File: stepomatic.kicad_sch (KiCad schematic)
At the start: 31 parts, among them J1 I2C, J4 USB_B_Micro, Q1 MMBT3904, Q2 MMBT3904, SW1 Mode, SW2 RST, U1 HDC1080DMBR, U2 AMS1117-3.3, U3 ULN2003A, U4 CH340C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

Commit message: Add JLC part for neopixel
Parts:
- D1: LCSC DNP -> C2843785
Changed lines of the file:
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@@
       (effects (font (size 1.27 1.27)) (justify left top) hide)
     )
-    (property "LCSC" "DNP" (id 5) (at 189.23 38.1 0)
+    (property "LCSC" "C2843785" (id 5) (at 189.23 38.1 0)
       (effects (font (size 1.27 1.27)) hide)
     )

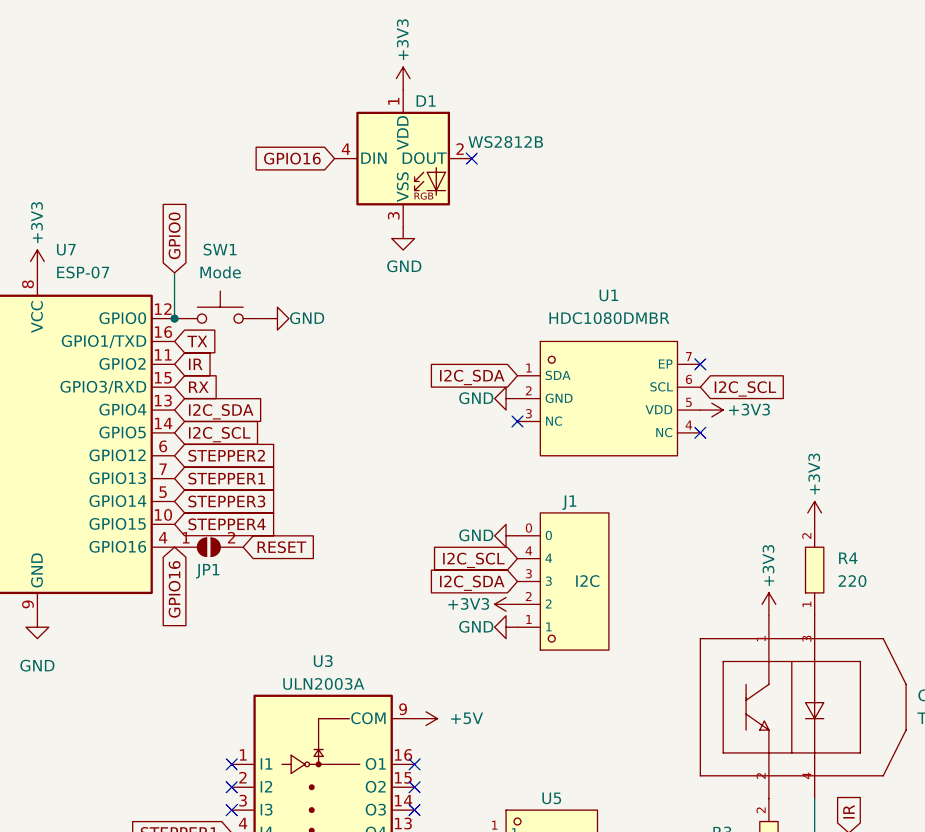
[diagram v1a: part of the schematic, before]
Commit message: Add EP pad of HDC1080DMBR
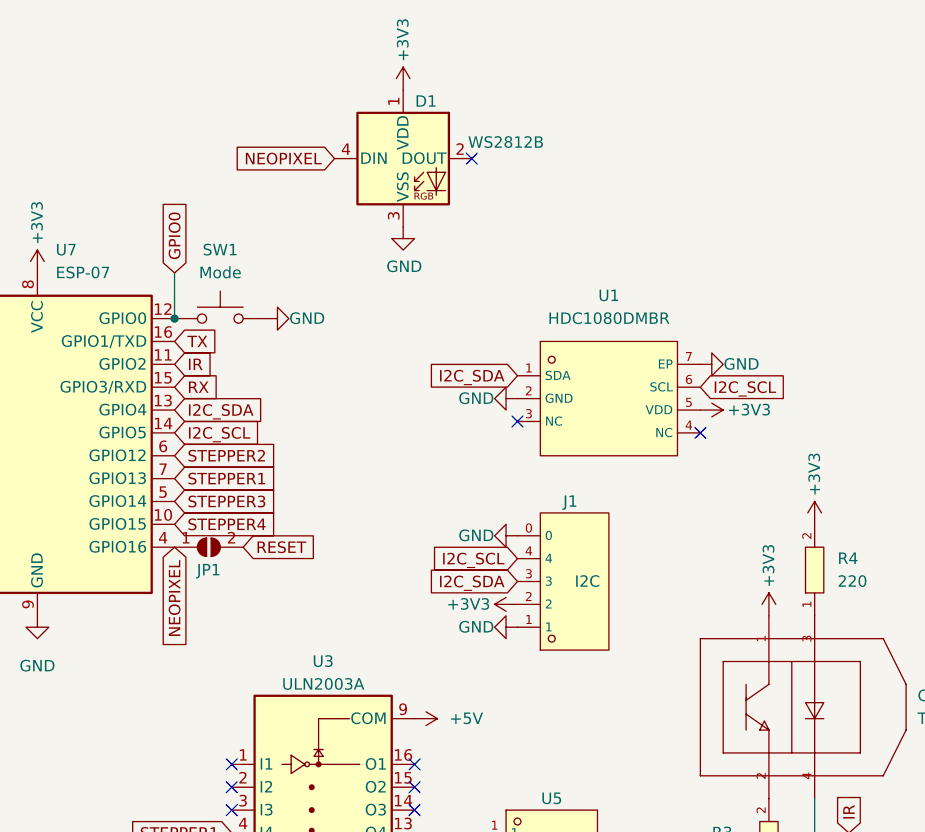
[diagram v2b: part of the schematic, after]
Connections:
- net GND: now also U1.7 (EP)
- net GPIO16 renamed NEOPIXEL
- no-connect marks 17 -> 16
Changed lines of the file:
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@@
   (no_connect (at 190.5 107.95))
   (no_connect (at 222.25 68.58))
-  (no_connect (at 222.25 60.96))
   (no_connect (at 81.28 73.66))
   (no_connect (at 190.5 105.41))
@@
     )
   )
-  (global_label "GPIO16" (shape input) (at 163.83 81.28 270) (fields_autoplaced)
+  (global_label "NEOPIXEL" (shape input) (at 163.83 81.28 270) (fields_autoplaced)
     (effects (font (size 1.27 1.27)) (justify right))
-    (property "Intersheet References" "${INTERSHEET_REFS}" (id 0) (at 163.7506 90.5874 90)
+    (property "Intersheet References" "${INTERSHEET_REFS}" (id 0) (at 163.7506 92.7645 90)
       (effects (font (size 1.27 1.27)) (justify right) hide)
     )
@@
     )
   )
-  (global_label "GPIO16" (shape input) (at 181.61 38.1 180) (fields_autoplaced)
+  (global_label "NEOPIXEL" (shape input) (at 181.61 38.1 180) (fields_autoplaced)
     (effects (font (size 1.27 1.27)) (justify right))
-    (property "Intersheet References" "${INTERSHEET_REFS}" (id 0) (at 172.3026 38.0206 0)
+    (property "Intersheet References" "${INTERSHEET_REFS}" (id 0) (at 170.1255 38.0206 0)
       (effects (font (size 1.27 1.27)) (justify right) hide)
     )
@@
     (pin "4")
   )
+  (symbol (lib_id "power:GND") (at 222.25 60.96 90) (unit 1)
+    (in_bom yes) (on_board yes)
+    (property "Reference" "#PWR0111" (id 0) (at 228.6 60.96 0)
+      (effects (font (size 1.27 1.27)) hide)
+    )
+    (property "Value" "GND" (id 1) (at 226.822 60.96 90))
+    (property "Footprint" "" (id 2) (at 222.25 60.96 0)
+      (effects (font (size 1.27 1.27)) hide)
+    )
+    (property "Datasheet" "" (id 3) (at 222.25 60.96 0)
+      (effects (font (size 1.27 1.27)) hide)
+    )
+    (pin "1")
+  )
   (symbol (lib_id "power:GND") (at 201.93 64.77 270) (unit 1)
     (in_bom yes) (on_board yes)
@@
       (reference "#PWR0110") (unit 1) (value "GND") (footprint "")
     )
+    (path "/f3e5bab0-c824-4fb9-ab63-26b208733bd7"
+      (reference "#PWR0111") (unit 1) (value "GND") (footprint "")
+    )
     (path "/f79577be-2482-43ec-a3db-27da2785cb91"

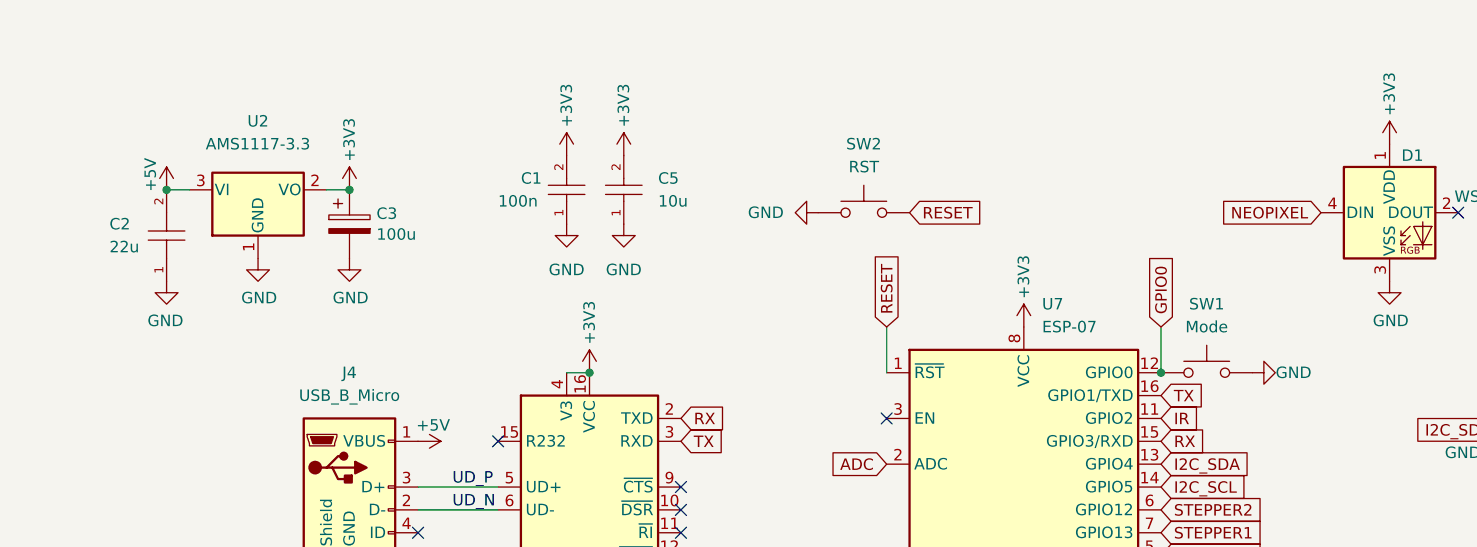
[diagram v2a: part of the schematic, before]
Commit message: Only use JLC footprints
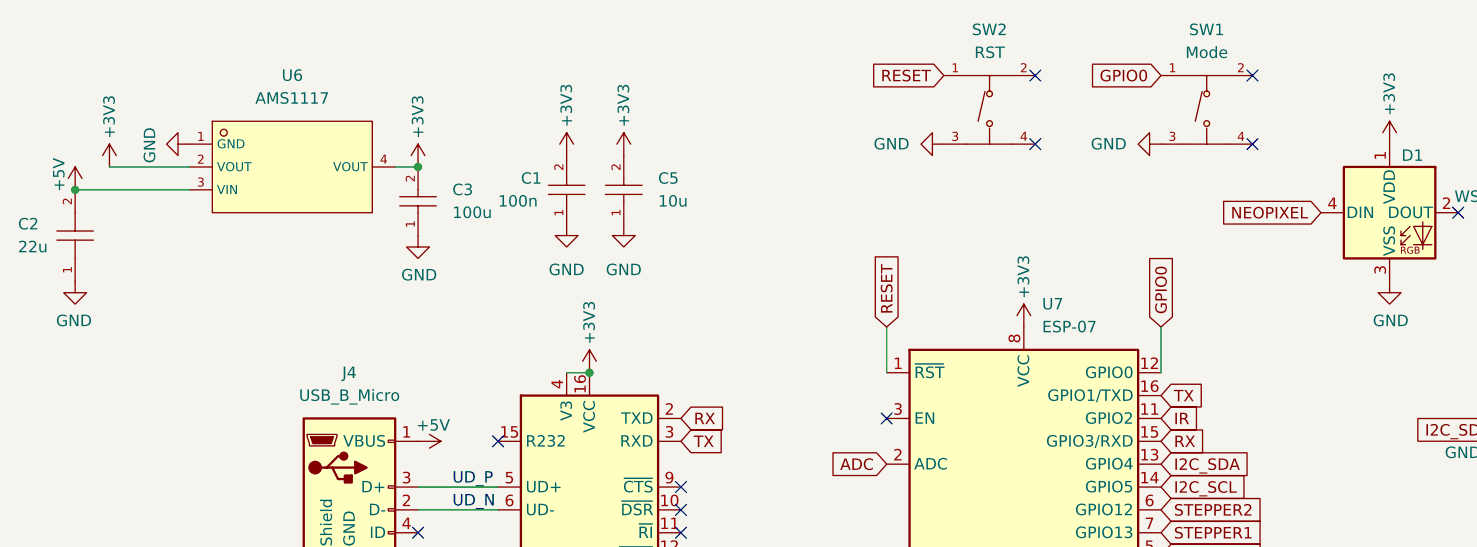
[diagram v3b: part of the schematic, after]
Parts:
- removed C3: 100u, footprint:C1206, symbol ESP-12E-breakout-rescue:CP-Device
- removed SW1: Mode, Button_Switch_SMD:SW_SPST_SKQG_WithoutStem, symbol Switch:SW_Push
- removed SW2: RST, Button_Switch_SMD:SW_SPST_SKQG_WithoutStem, symbol Switch:SW_Push
- removed U2: AMS1117-3.3, Package_TO_SOT_SMD:SOT-223-3_TabPin2, symbol Regulator_Linear:AMS1117-3.3
- added C3: 100u, footprint:C1206, symbol CL31A107MQHNNNE:CL31A107MQHNNNE
- added SW1: Mode, footprint:SW-SMD_4P-L5.1-W5.1-P3.70-LS6.5-TL-2, symbol TS-1187A-B-A-B:TS-1187A-B-A-B
- added SW2: RST, footprint:SW-SMD_4P-L5.1-W5.1-P3.70-LS6.5-TL-2, symbol TS-1187A-B-A-B:TS-1187A-B-A-B
- added U6: AMS1117, footprint:SOT-223-3_L6.5-W3.4-P2.30-LS7.0-BR, symbol AMS1117-3_3:AMS1117-3_3
- U3: footprint Package_SO:SOP-16_4.55x10.3mm_P1.27mm -> footprint:SOIC-16_L9.9-W3.9-P1.27-LS6.0-BL
- U4: footprint Package_SO:SOIC-16_3.9x9.9mm_P1.27mm -> footprint:SOP-16_L10.0-W3.9-P1.27-LS6.0-BL
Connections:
- net +3V3: now also C3.2, U6.2 (VOUT), U6.4 (VOUT)
- net +5V: now also U6.3 (VIN)
- net GND: now also C3.1, SW1.3 (C), SW2.3 (C), U6.1 (GND)
- net GPIO0: now also SW1.1 (A)
- net RESET: now also SW2.1 (A)
- no-connect marks 16 -> 20
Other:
- moved on the sheet: C2

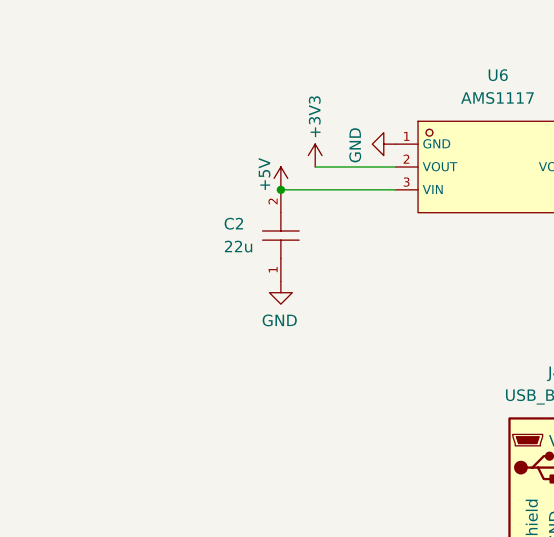
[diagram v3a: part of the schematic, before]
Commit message: Add pcb artwork and some 5V caps
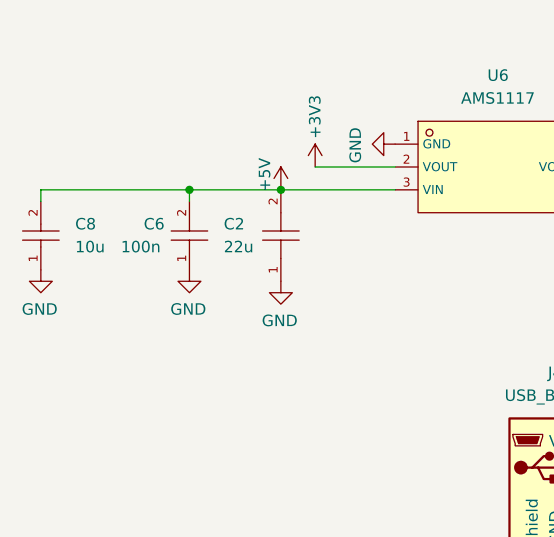
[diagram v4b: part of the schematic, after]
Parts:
- added C6: 100n, footprint:C0402, symbol CL05B104KO5NNNC:CL05B104KO5NNNC
- added C8: 10u, footprint:C0402, symbol CL05A106MQ5NUNC:CL05A106MQ5NUNC
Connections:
- net +5V: now also C6.2, C8.2
- net GND: now also C6.1, C8.1
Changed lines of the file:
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@@
   (junction (at 81.28 33.02) (diameter 0) (color 0 0 0 0)
+  )
+  (junction (at 33.02 35.56) (diameter 0) (color 0 0 0 0)
   )
   (no_connect (at 196.85 38.1))
@@
     (stroke (width 0) (type default) (color 0 0 0 0))
   )
+  (wire (pts (xy 16.51 35.56) (xy 33.02 35.56))
+    (stroke (width 0) (type default) (color 0 0 0 0))
+  )
+  (wire (pts (xy 33.02 35.56) (xy 43.18 35.56))
+    (stroke (width 0) (type default) (color 0 0 0 0))
+  )
   (wire (pts (xy 78.74 33.02) (xy 81.28 33.02))
     (stroke (width 0) (type default) (color 0 0 0 0))
@@
     (stroke (width 0) (type default) (color 0 0 0 0))
   )
+  (wire (pts (xy 16.51 36.83) (xy 16.51 35.56))
+    (stroke (width 0) (type default) (color 0 0 0 0))
+  )
   (wire (pts (xy 163.83 50.8) (xy 163.83 55.88))
     (stroke (width 0) (type default) (color 0 0 0 0))
@@
   )
   (wire (pts (xy 81.28 68.58) (xy 90.17 68.58))
+    (stroke (width 0) (type default) (color 0 0 0 0))
+  )
+  (wire (pts (xy 33.02 36.83) (xy 33.02 35.56))
     (stroke (width 0) (type default) (color 0 0 0 0))
   )
@@
     )
   )
+  (symbol (lib_id "power:GND") (at 16.51 44.45 0) (mirror y) (unit 1)
+    (in_bom yes) (on_board yes)
+    (property "Reference" "#PWR03" (id 0) (at 16.51 50.8 0)
+      (effects (font (size 1.27 1.27)) hide)
+    )
+    (property "Value" "GND" (id 1) (at 16.383 48.8442 0))
+    (property "Footprint" "" (id 2) (at 16.51 44.45 0)
+      (effects (font (size 1.27 1.27)) hide)
+    )
+    (property "Datasheet" "" (id 3) (at 16.51 44.45 0)
+      (effects (font (size 1.27 1.27)) hide)
+    )
+    (pin "1")
+  )
   (symbol (lib_name "GND_1") (lib_id "power:GND") (at 133.35 97.79 0) (unit 1)
     (in_bom yes) (on_board yes) (fields_autoplaced)
@@
     (pin "3")
     (pin "4")
+  )
+  (symbol (lib_id "power:GND") (at 33.02 44.45 0) (mirror y) (unit 1)
+    (in_bom yes) (on_board yes)
+    (property "Reference" "#PWR0131" (id 0) (at 33.02 50.8 0)
+      (effects (font (size 1.27 1.27)) hide)
+    )
+    (property "Value" "GND" (id 1) (at 32.893 48.8442 0))
+    (property "Footprint" "" (id 2) (at 33.02 44.45 0)
+      (effects (font (size 1.27 1.27)) hide)
+    )
+    (property "Datasheet" "" (id 3) (at 33.02 44.45 0)
+      (effects (font (size 1.27 1.27)) hide)
+    )
+    (pin "1")
   )
   (symbol (lib_id "power:+5V") (at 43.18 35.56 0) (mirror y) (unit 1)
@@
     (pin "9")
   )
+  (symbol (lib_id "CL05A106MQ5NUNC:CL05A106MQ5NUNC") (at 16.51 40.64 90) (unit 1)
+    (in_bom yes) (on_board yes) (fields_autoplaced)
+    (property "Reference" "C8" (id 0) (at 20.32 39.3699 90)
+      (effects (font (size 1.27 1.27)) (justify right))
+    )
+    (property "Value" "10u" (id 1) (at 20.32 41.9099 90)
+      (effects (font (size 1.27 1.27)) (justify right))
+    )
+    (property "Footprint" "footprint:C0402" (id 2) (at 26.67 40.64 0)
+      (effects (font (size 1.27 1.27) italic) hide)
+    )
+    (property "Datasheet" "https://item.szlcsc.com/15869.html" (id 3) (at 16.383 42.926 0)
+      (effects (font (size 1.27 1.27)) (justify left) hide)
+    )
+    (property "LCSC" "C15525" (id 4) (at 16.51 40.64 0)
+      (effects (font (size 1.27 1.27)) hide)
+    )
+    (pin "1")
+    (pin "2")
+  )
   (symbol (lib_id "TCRT5000L:TCRT5000L") (at 232.41 99.06 0) (unit 1)
     (in_bom yes) (on_board yes) (fields_autoplaced)
@@
     )
     (pin "1")
+  )
+  (symbol (lib_id "CL05B104KO5NNNC:CL05B104KO5NNNC") (at 33.02 40.64 90) (unit 1)
+    (in_bom yes) (on_board yes)
+    (property "Reference" "C6" (id 0) (at 27.94 39.37 90)
+      (effects (font (size 1.27 1.27)) (justify right))
+    )
+    (property "Value" "100n" (id 1) (at 25.4 41.91 90)
+      (effects (font (size 1.27 1.27)) (justify right))
+    )
+    (property "Footprint" "footprint:C0402" (id 2) (at 43.18 40.64 0)
+      (effects (font (size 1.27 1.27) italic) hide)
+    )
+    (property "Datasheet" "https://item.szlcsc.com/15869.html" (id 3) (at 32.893 42.926 0)
+      (effects (font (size 1.27 1.27)) (justify left) hide)
+    )
+    (property "LCSC" "C1525" (id 4) (at 33.02 40.64 0)
+      (effects (font (size 1.27 1.27)) hide)
+    )
+    (pin "1")
+    (pin "2")
   )
   (symbol (lib_id "power:+3V3") (at 81.28 33.02 0) (mirror y) (unit 1)
@@
       (reference "#PWR02") (unit 1) (value "+3V3") (footprint "")
     )
+    (path "/1307bcd8-ff24-4878-ac18-7726b6022aa3"
+      (reference "#PWR03") (unit 1) (value "GND") (footprint "")
+    )
     (path "/6fe1ffb2-d913-4a5c-9eb8-7ec1ce5ccba3"
       (reference "#PWR04") (unit 1) (value "+3V3") (footprint "")
@@
       (reference "#PWR0130") (unit 1) (value "GND") (footprint "")
     )
+    (path "/87cde4a8-3b39-43a9-96da-07859c48449e"
+      (reference "#PWR0131") (unit 1) (value "GND") (footprint "")
+    )
     (path "/3f6189a4-1124-4aa2-a3da-8258067ed27d"
       (reference "C1") (unit 1) (value "100n") (footprint "footprint:C0402")
@@
       (reference "C5") (unit 1) (value "10u") (footprint "footprint:C0402")
     )
+    (path "/fa66d18d-9f61-4f33-ad54-8fb27a84dd43"
+      (reference "C6") (unit 1) (value "100n") (footprint "footprint:C0402")
+    )
     (path "/933916de-b71d-4075-aeaa-70806e65c708"
       (reference "C7") (unit 1) (value "10u") (footprint "footprint:C0402")
     )
+    (path "/ecc4b49e-cb78-4bd2-9d56-3c56c1ab334c"
+      (reference "C8") (unit 1) (value "10u") (footprint "footprint:C0402")
+    )
     (path "/f05ece95-91de-4028-9504-1af74c7fda14"
